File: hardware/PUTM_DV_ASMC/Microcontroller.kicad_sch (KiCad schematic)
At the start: 29 parts, among them U1 LM4040C33FTA, U2 STM32G484RETx, Y1 ATX-11-F-32.000MHZ-F05-T

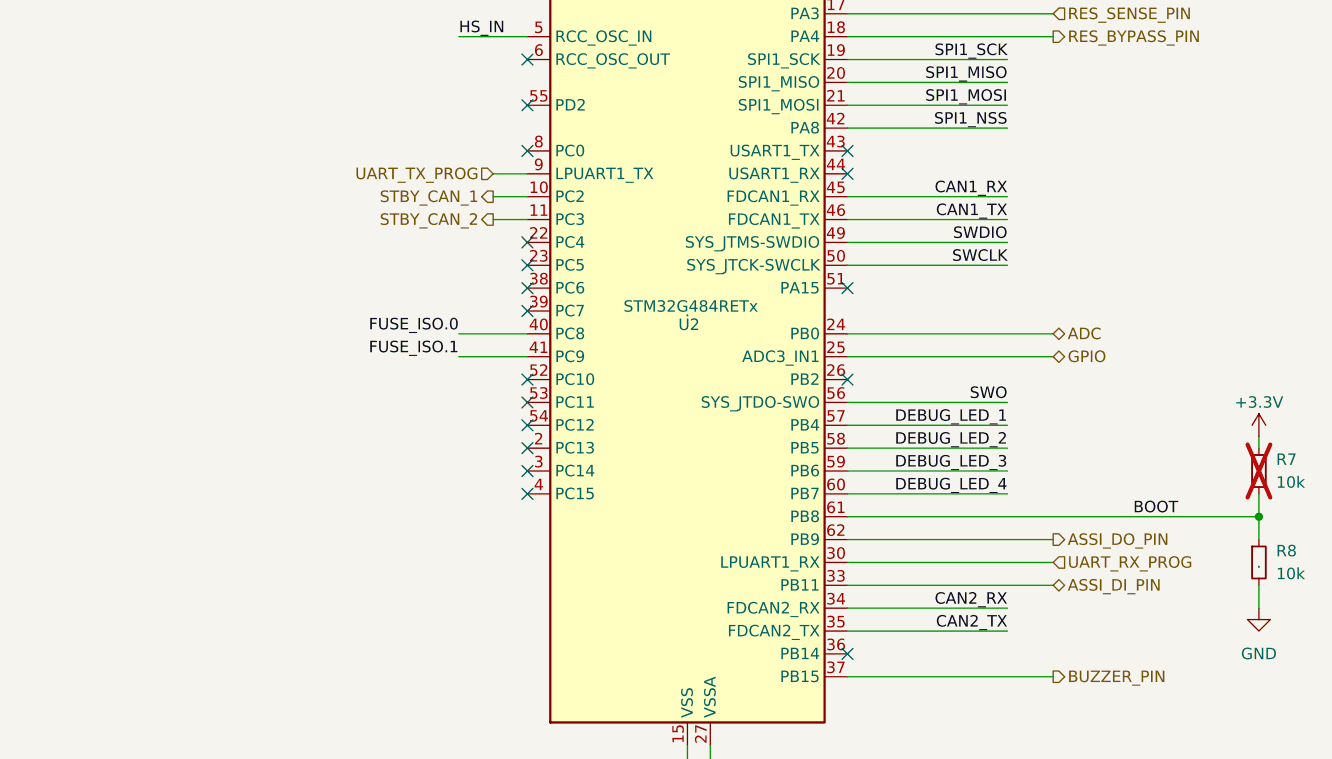
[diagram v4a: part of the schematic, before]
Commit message: update pins mcu
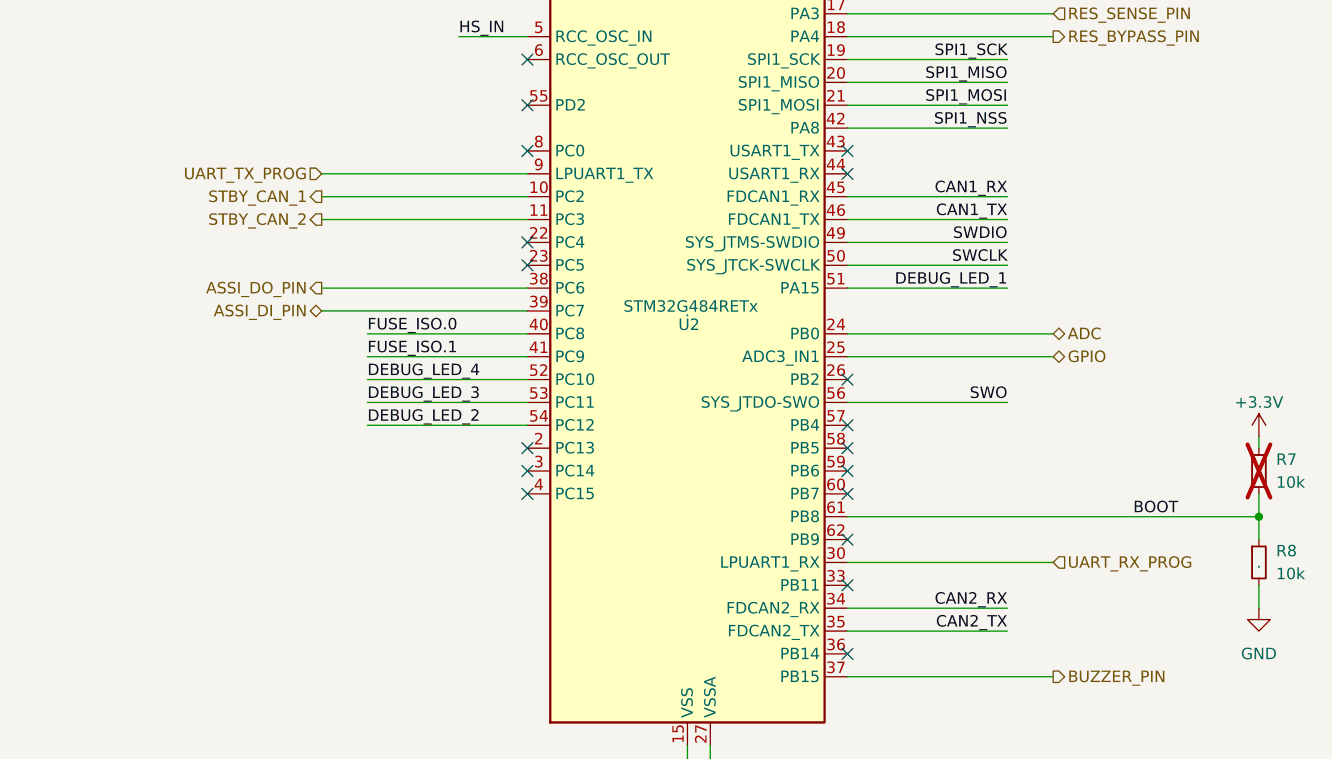
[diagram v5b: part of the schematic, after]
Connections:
- net ASSI_DI_PIN: now also U2.39 (PC7); no longer U2.33 (PB11)
- net ASSI_DO_PIN: now also U2.38 (PC6); no longer U2.62 (PB9)
- net DEBUG_LED_1: now also U2.51 (PA15); no longer U2.57 (PB4)
- net DEBUG_LED_2: now also U2.54 (PC12); no longer U2.58 (PB5)
- net DEBUG_LED_3: now also U2.53 (PC11); no longer U2.59 (PB6)
- net DEBUG_LED_4: now also U2.52 (PC10); no longer U2.60 (PB7)
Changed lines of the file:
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@@
 	)
 	(no_connect
-		(at 198.12 93.98)
+		(at 233.68 127)
+	)
+	(no_connect
+		(at 233.68 121.92)
 	)
 	(no_connect
@@
 	)
 	(no_connect
+		(at 233.68 111.76)
+	)
+	(no_connect
 		(at 198.12 78.74)
 	)
@@
 	)
 	(no_connect
+		(at 233.68 116.84)
+	)
+	(no_connect
 		(at 198.12 116.84)
 	)
@@
 	)
 	(no_connect
-		(at 233.68 93.98)
+		(at 233.68 78.74)
 	)
 	(no_connect
-		(at 233.68 78.74)
-	)
-	(no_connect
-		(at 198.12 96.52)
+		(at 233.68 109.22)
 	)
 	(no_connect
@@
 	)
 	(no_connect
+		(at 233.68 114.3)
+	)
+	(no_connect
 		(at 198.12 114.3)
 	)
 	(no_connect
 		(at 198.12 111.76)
-	)
-	(no_connect
-		(at 198.12 106.68)
-	)
-	(no_connect
-		(at 198.12 104.14)
-	)
-	(no_connect
-		(at 198.12 109.22)
 	)
 	(bus_entry
@@
 	(wire
 		(pts
-			(xy 233.68 116.84) (xy 251.46 116.84)
-		)
-		(stroke
-			(width 0)
-			(type default)
-		)
-	)
-	(wire
-		(pts
 			(xy 210.82 33.02) (xy 198.12 33.02)
 		)
@@
 	(wire
 		(pts
-			(xy 233.68 109.22) (xy 251.46 109.22)
-		)
-		(stroke
-			(width 0)
-			(type default)
-		)
-	)
-	(wire
-		(pts
-			(xy 233.68 121.92) (xy 256.54 121.92)
-		)
-		(stroke
-			(width 0)
-			(type default)
-		)
-	)
-	(wire
-		(pts
 			(xy 233.68 99.06) (xy 256.54 99.06)
 		)
@@
 	(wire
 		(pts
+			(xy 198.12 93.98) (xy 175.26 93.98)
+		)
+		(stroke
+			(width 0)
+			(type default)
+		)
+	)
+	(wire
+		(pts
 			(xy 236.22 33.02) (xy 223.52 33.02)
 		)
@@
 	(wire
 		(pts
-			(xy 190.5 99.06) (xy 198.12 99.06)
+			(xy 180.34 99.06) (xy 198.12 99.06)
 		)
 		(stroke
@@
 	(wire
 		(pts
+			(xy 198.12 104.14) (xy 180.34 104.14)
+		)
+		(stroke
+			(width 0)
+			(type default)
+		)
+	)
+	(wire
+		(pts
 			(xy 26.67 34.29) (xy 38.1 34.29)
 		)
@@
 	(wire
 		(pts
-			(xy 233.68 114.3) (xy 251.46 114.3)
+			(xy 198.12 109.22) (xy 180.34 109.22)
 		)
 		(stroke
@@
 	(wire
 		(pts
-			(xy 233.68 127) (xy 256.54 127)
-		)
-		(stroke
-			(width 0)
-			(type default)
-		)
-	)
-	(wire
-		(pts
 			(xy 236.22 21.59) (xy 245.11 21.59)
 		)
@@
 	(wire
 		(pts
+			(xy 233.68 93.98) (xy 251.46 93.98)
+		)
+		(stroke
+			(width 0)
+			(type default)
+		)
+	)
+	(wire
+		(pts
 			(xy 233.68 132.08) (xy 251.46 132.08)
 		)
@@
 	(wire
 		(pts
-			(xy 194.31 81.28) (xy 198.12 81.28)
+			(xy 175.26 81.28) (xy 198.12 81.28)
 		)
 		(stroke
@@
 	(wire
 		(pts
+			(xy 198.12 96.52) (xy 175.26 96.52)
+		)
+		(stroke
+			(width 0)
+			(type default)
+		)
+	)
+	(wire
+		(pts
 			(xy 259.08 21.59) (xy 259.08 24.13)
 		)
@@
 	(wire
 		(pts
+			(xy 198.12 106.68) (xy 180.34 106.68)
+		)
+		(stroke
+			(width 0)
+			(type default)
+		)
+	)
+	(wire
+		(pts
 			(xy 87.63 189.23) (xy 96.52 189.23)
 		)
@@
 	(wire
 		(pts
-			(xy 190.5 101.6) (xy 198.12 101.6)
+			(xy 180.34 101.6) (xy 198.12 101.6)
 		)
 		(stroke
@@
 	(wire
 		(pts
-			(xy 194.31 86.36) (xy 198.12 86.36)
+			(xy 175.26 86.36) (xy 198.12 86.36)
 		)
 		(stroke
@@
 	(wire
 		(pts
-			(xy 233.68 111.76) (xy 251.46 111.76)
-		)
-		(stroke
-			(width 0)
-			(type default)
-		)
-	)
-	(wire
-		(pts
 			(xy 114.3 34.29) (xy 118.11 34.29)
 		)
@@
 	(wire
 		(pts
-			(xy 194.31 83.82) (xy 198.12 83.82)
+			(xy 175.26 83.82) (xy 198.12 83.82)
 		)
 		(stroke
@@
 	)
 	(label "FUSE_ISO.0"
-		(at 190.5 99.06 180)
-		(effects
-			(font
-				(size 1.27 1.27)
-			)
-			(justify right bottom)
+		(at 180.34 99.06 0)
+		(effects
+			(font
+				(size 1.27 1.27)
+			)
+			(justify left bottom)
 		)
 	)
@@
 		)
 	)
-	(label "DEBUG_LED_4"
-		(at 251.46 116.84 180)
-		(effects
-			(font
-				(size 1.27 1.27)
-			)
-			(justify right bottom)
-		)
-	)
 	(label "BOOT"
 		(at 265.43 119.38 0)
@@
 		)
 	)
-	(label "DEBUG_LED_2"
-		(at 251.46 111.76 180)
-		(effects
-			(font
-				(size 1.27 1.27)
-			)
-			(justify right bottom)
-		)
-	)
 	(label "CAN2_TX"
 		(at 251.46 132.08 180)
@@
 		)
 	)
+	(label "DEBUG_LED_4"
+		(at 180.34 104.14 0)
+		(effects
+			(font
+				(size 1.27 1.27)
+			)
+			(justify left bottom)
+		)
+	)
 	(label "SWDIO"
 		(at 87.63 177.8 180)
@@
 		)
 	)
-	(label "DEBUG_LED_1"
-		(at 251.46 109.22 180)
-		(effects
-			(font
-				(size 1.27 1.27)
-			)
-			(justify right bottom)
-		)
-	)
 	(label "CAN1_TX"
 		(at 251.46 86.36 180)
@@
 		)
 	)
+	(label "DEBUG_LED_1"
+		(at 251.46 93.98 180)
+		(effects
+			(font
+				(size 1.27 1.27)
+			)
+			(justify right bottom)
+		)
+	)
 	(label "CAN2_RX"
 		(at 251.46 129.54 180)
@@
 	)
 	(label "FUSE_ISO.1"
-		(at 190.5 101.6 180)
-		(effects
-			(font
-				(size 1.27 1.27)
-			)
-			(justify right bottom)
+		(at 180.34 101.6 0)
+		(effects
+			(font
+				(size 1.27 1.27)
+			)
+			(justify left bottom)
 		)
 	)
@@
 	)
 	(label "DEBUG_LED_3"
-		(at 251.46 114.3 180)
-		(effects
-			(font
-				(size 1.27 1.27)
-			)
-			(justify right bottom)
-		)
-	)
-	(label "DEBUG_LED_3"
 		(at 46.355 136.525 0)
 		(effects
@@
 		)
 	)
+	(label "DEBUG_LED_3"
+		(at 180.34 106.68 0)
+		(effects
+			(font
+				(size 1.27 1.27)
+			)
+			(justify left bottom)
+		)
+	)
 	(label "FUSE_ISO.1"
 		(at 87.63 109.22 180)
@@
 		)
 	)
+	(label "DEBUG_LED_2"
+		(at 180.34 109.22 0)
+		(effects
+			(font
+				(size 1.27 1.27)
+			)
+			(justify left bottom)
+		)
+	)
 	(label "SPI1_MOSI"
 		(at 251.46 73.66 180)
@@
 	(hierarchical_label "STBY_CAN_2"
 		(shape output)
-		(at 194.31 86.36 180)
+		(at 175.26 86.36 180)
 		(effects
 			(font
@@
 		)
 	)
-	(hierarchical_label "ASSI_DI_PIN"
-		(shape bidirectional)
-		(at 256.54 127 0)
-		(effects
-			(font
-				(size 1.27 1.27)
-			)
-			(justify left)
-		)
-	)
 	(hierarchical_label "STBY_CAN_1"
 		(shape output)
-		(at 194.31 83.82 180)
+		(at 175.26 83.82 180)
 		(effects
 			(font
@@
 	(hierarchical_label "UART_TX_PROG"
 		(shape input)
-		(at 194.31 81.28 180)
+		(at 175.26 81.28 180)
 		(effects
 			(font
@@
 		)
 	)
+	(hierarchical_label "ASSI_DO_PIN"
+		(shape output)
+		(at 175.26 93.98 180)
+		(effects
+			(font
+				(size 1.27 1.27)
+			)
+			(justify right)
+		)
+	)
 	(hierarchical_label "FUSE_ISO{FUSE_ISO.0 FUSE_ISO.1}"
 		(shape input)
@@
 		)
 	)
-	(hierarchical_label "ASSI_DO_PIN"
-		(shape output)
-		(at 256.54 121.92 0)
-		(effects
-			(font
-				(size 1.27 1.27)
-			)
-			(justify left)
-		)
-	)
 	(hierarchical_label "{ST_LINK}"
 		(shape bidirectional)
@@
 		)
 	)
+	(hierarchical_label "ASSI_DI_PIN"
+		(shape bidirectional)
+		(at 175.26 96.52 180)
+		(effects
+			(font
+				(size 1.27 1.27)
+			)
+			(justify right)
+		)
+	)

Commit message: work on supply and zones
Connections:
- net +3.3V renamed +3V3
- net FUSE_ISO.0 renamed FUSE_IS0
- net FUSE_ISO.1 renamed FUSE_IS1
- net LHI.0 renamed LHI0
- net LHI.1 renamed LHI1
- net SPI1_MISO renamed SPI1.MISO
- net SPI1_MOSI renamed SPI1.MOSI
- net SPI1_NSS renamed SPI1.NSS
- net SPI1_SCK renamed SPI1.SCK
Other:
- moved on the sheet: D1, D2, D3, D4, R2, R3, R4, R5

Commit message: work work work
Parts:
- removed TP1: TestPoint_Small, TestPoint:TestPoint_THTPad_D1.0mm_Drill0.5mm, symbol Connector:TestPoint_Small
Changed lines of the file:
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@@
 		)
 	)
-	(label "CAN2_TX"
-		(at 251.46 132.08 180)
-		(effects
-			(font
-				(size 1.27 1.27)
-			)
-			(justify right bottom)
-		)
-	)
 	(label "SPI1.MISO"
 		(at 251.46 71.12 180)
@@
 		)
 	)
-	(label "CAN1_RX"
-		(at 251.46 83.82 180)
-		(effects
-			(font
-				(size 1.27 1.27)
-			)
-			(justify right bottom)
-		)
-	)
 	(label "SWCLK"
 		(at 87.63 181.61 180)
@@
 		)
 	)
-	(label "CAN1_TX"
-		(at 251.46 86.36 180)
-		(effects
-			(font
-				(size 1.27 1.27)
-			)
-			(justify right bottom)
-		)
-	)
 	(label "SWDIO"
 		(at 251.46 88.9 180)
@@
 		)
 	)
-	(label "CAN2_RX"
-		(at 251.46 129.54 180)
-		(effects
-			(font
-				(size 1.27 1.27)
-			)
-			(justify right bottom)
-		)
-	)
 	(label "SPI1.MISO"
 		(at 86.36 133.35 180)
@@
 		)
 	)
+	(label "CAN2_TX"
+		(at 251.46 132.08 180)
+		(effects
+			(font
+				(size 1.27 1.27)
+			)
+			(justify right bottom)
+		)
+	)
 	(label "VREF"
 		(at 190.5 55.88 0)
@@
 		)
 	)
+	(label "CAN1_RX"
+		(at 251.46 83.82 180)
+		(effects
+			(font
+				(size 1.27 1.27)
+			)
+			(justify right bottom)
+		)
+	)
 	(label "LHI0"
 		(at 251.46 55.88 180)
@@
 		)
 	)
+	(label "CAN1_TX"
+		(at 251.46 86.36 180)
+		(effects
+			(font
+				(size 1.27 1.27)
+			)
+			(justify right bottom)
+		)
+	)
 	(label "SPI1.NSS"
 		(at 251.46 76.2 180)
@@
 		)
 	)
+	(label "CAN2_RX"
+		(at 251.46 129.54 180)
+		(effects
+			(font
+				(size 1.27 1.27)
+			)
+			(justify right bottom)
+		)
+	)
 	(label "DEBUG_LED_2"
 		(at 49.53 127 0)
@@
 		)
 	)
-	(hierarchical_label "{ST_LINK}"
-		(shape bidirectional)
+	(hierarchical_label "{ST-LINK}"
+		(shape input)
 		(at 111.76 165.1 0)
 		(effects
@@
 					(unit 1)
 				)
-			)
-		)
-	)
-	(symbol
-		(lib_id "Connector:TestPoint_Small")
-		(at 38.1 34.29 0)
-		(unit 1)
-		(body_style 1)
-		(exclude_from_sim no)
-		(in_bom yes)
-		(on_board yes)
-		(in_pos_files yes)
-		(dnp no)
-		(property "Reference" "TP1"
-			(at 34.29 33.02 0)
-			(show_name no)
-			(do_not_autoplace no)
-			(effects
-				(font
-					(size 1 1)
-				)
-				(justify left)
-			)
-		)
-		(property "Value" "TestPoint_Small"
-			(at 39.37 36.195 0)
-			(hide yes)
-			(show_name no)
-			(do_not_autoplace no)
-			(effects
-				(font
-					(size 1.27 1.27)
-				)
-				(justify left)
-			)
-		)
-		(property "Footprint" "TestPoint:TestPoint_THTPad_D1.0mm_Drill0.5mm"
-			(at 43.18 34.29 0)
-			(hide yes)
-			(show_name no)
-			(do_not_autoplace no)
-			(effects
-				(font
-					(size 1.27 1.27)
-				)
-			)
-		)
-		(property "Datasheet" ""
-			(at 43.18 34.29 0)
-			(hide yes)
-			(show_name no)
-			(do_not_autoplace no)
-			(effects
-				(font
-					(size 1.27 1.27)
-				)
-			)
-		)
-		(property "Description" ""
-			(at 38.1 34.29 0)
-			(hide yes)
-			(show_name no)
-			(do_not_autoplace no)
-			(effects
-				(font
-					(size 1.27 1.27)
-				)
-			)
-		)
-		(pin "1"
-		)
-		(instances
-			(project "PUTM_DV_ASMC"
-				(path "/b652b05a-4e3d-4ad1-b032-18886abe7d45/e9155621-e51e-4c8e-b02a-95579a590de1"
-					(reference "TP1")
-					(unit 1)
-				)

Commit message: can layout
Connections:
- net DEBUG_LED_1: now also U2.54 (PC12); no longer U2.51 (PA15)
- net DEBUG_LED_2: now also U2.53 (PC11); no longer U2.54 (PC12)
- net DEBUG_LED_3: now also U2.52 (PC10); no longer U2.53 (PC11)
- net DEBUG_LED_4: now also U2.51 (PA15); no longer U2.52 (PC10)
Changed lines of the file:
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@@
 		)
 	)
-	(label "DEBUG_LED_4"
+	(label "DEBUG_LED_3"
 		(at 180.34 104.14 0)
 		(effects
@@
 		)
 	)
-	(label "DEBUG_LED_1"
+	(label "DEBUG_LED_4"
 		(at 251.46 93.98 180)
 		(effects
@@
 		)
 	)
-	(label "DEBUG_LED_3"
+	(label "DEBUG_LED_2"
 		(at 180.34 106.68 0)
 		(effects
@@
 		)
 	)
-	(label "DEBUG_LED_2"
+	(label "DEBUG_LED_1"
 		(at 180.34 109.22 0)
 		(effects
